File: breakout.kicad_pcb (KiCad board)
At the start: 2 copper layers, 24.1 x 52.9 mm, 5 parts

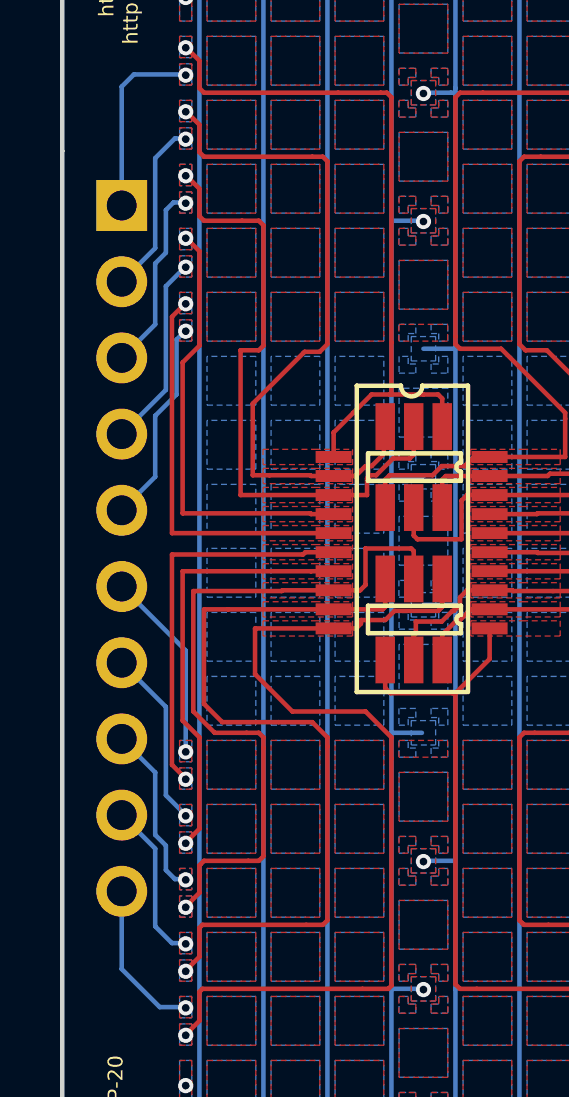
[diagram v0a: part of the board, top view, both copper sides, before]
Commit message: Moved left header slightly, it was misaligned.
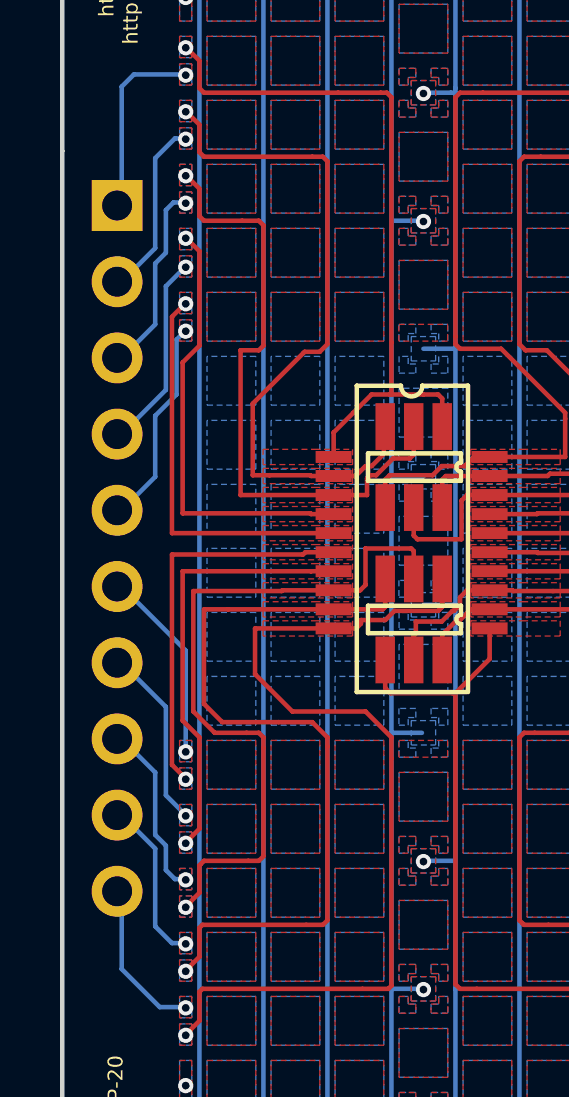
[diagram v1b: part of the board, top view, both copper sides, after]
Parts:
- moved ? 0.15 mm to (143.5, 82.0)
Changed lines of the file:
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@@
   )
   (module prototyping:PinHeader_1x10_P2.54mm_Vertical (layer F.Cu)
-    (at 143.6624 82.042)
+    (at 143.51 82.042)
     (descr "Through hole straight pin header, 1x10, 2.54mm pitch, single row")
     (tags "Through hole pin header THT 1x10 2.54mm single row")
